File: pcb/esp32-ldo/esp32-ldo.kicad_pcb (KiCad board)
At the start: 2 copper layers, 32 x 35.2 mm, 29 parts, among them J1 BATT, J2 PROG, J3 HALL, Q1 BC817, Q2 BC807, SW1 RST, U1 XC6220, U2 ESP32-WROOM-32D

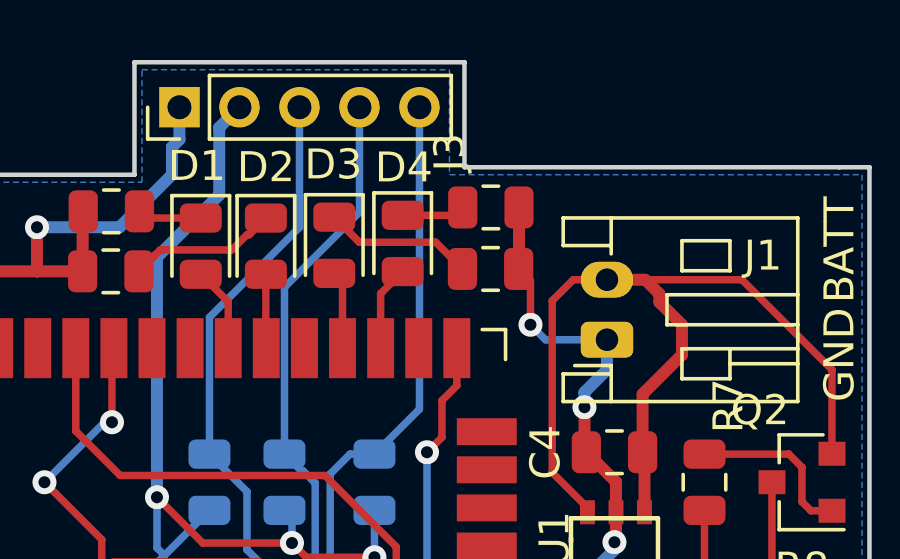
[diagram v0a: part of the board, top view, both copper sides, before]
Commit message: pcb: removed LED 4
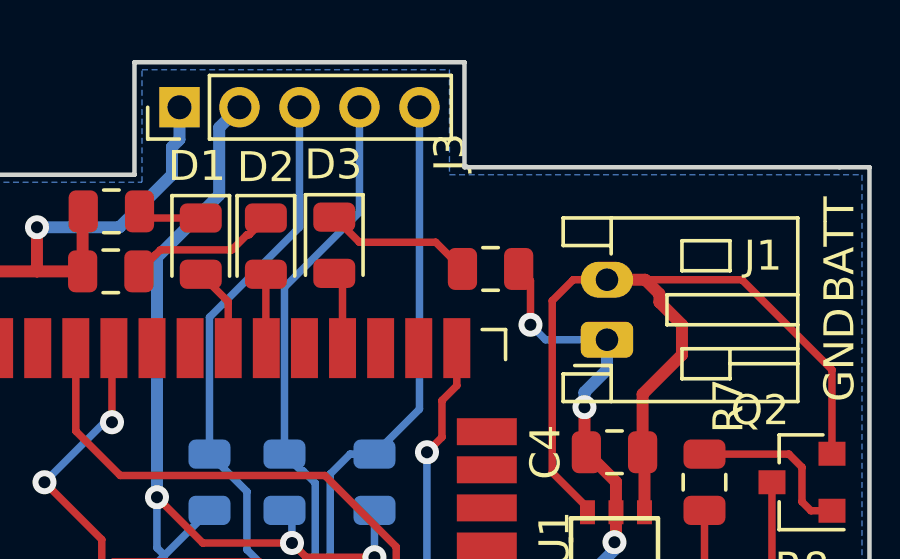
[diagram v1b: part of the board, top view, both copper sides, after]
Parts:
- removed D4: GREEN, LED_SMD:LED_0805_2012Metric
- removed R5: R, Resistor_SMD:R_0805_2012Metric
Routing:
- net Net-(U2-Pad27): track 2.86 -> 0.00 mm
- net Net-(D4-Pad1): track 2.11 -> 0.00 mm
- net GND: track 132.1 -> 130.0 mm
